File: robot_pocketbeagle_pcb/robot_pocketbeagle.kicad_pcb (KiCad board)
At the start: 2 copper layers, 75 x 100 mm, 104 parts, among them J1 QMC5883L, J10 driver_dvr8833, J12 IN_DVR8833, J13 9V_DC_DC, J14 servo_x_y, J15 shr05, J16 5V_DC_DC, J17 Conn_GND, J18 Conn_5V, J19 Conn_pwm_out_b, J2 USB_A, J20 Conn_pwm_out_a, J21 Conn_P2_3.3V, J29 Conn_AIN_4.096_3.3_1.8V, J3 UART0, J30 Conn_5V, J31 Conn_GPI028_34, J4 P1, J5 MPU6050, J6 ADS1115, J7 P2, J8 Conn_i2c2, J9 OUT_DVR8833, Q1 BC847, Q2 BC847, Q3 QM6015D, Q4 BC847, Q5 BC847, Q6 QM6015D, Q7 QM6015D, U1 PC817, U2 PC817, U3 74HC00, U4 LM358, U5 L7805_REZERV

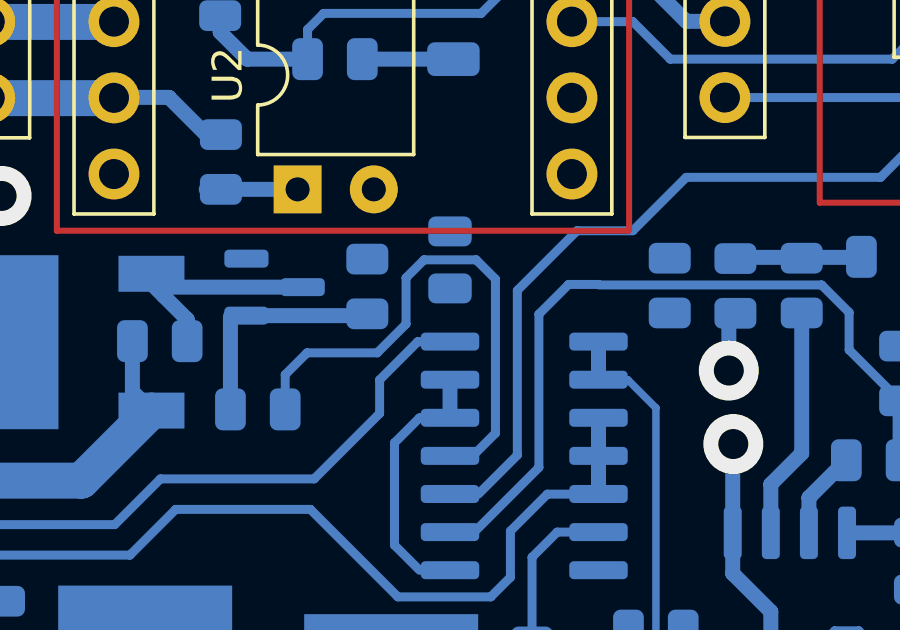
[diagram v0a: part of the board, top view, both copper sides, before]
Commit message: add doc and fix shem board
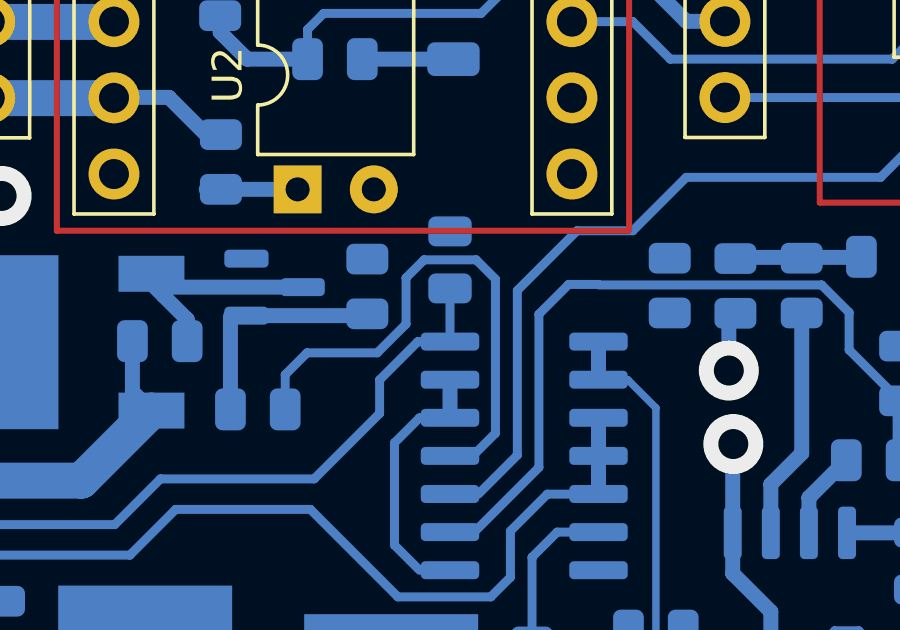
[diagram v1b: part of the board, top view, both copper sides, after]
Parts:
- C5: value 33n -> 330n
- C6: value 1n -> 100n
- R1, R2: value 1K -> 180
- R14: value 150K -> 1.5K
- R15: value 75K -> 750
- R16: value 430K -> 4.3K
- R17: value 100K -> 1K
- R18: value 110K -> 2k
- R21: value 100K -> 1.5k
- R30: value 110K -> 2K
- R31: value 100K -> 1.5K
- R41: value 2K -> 350
- R8: value 3K -> 3.3K
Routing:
- net AUX_5V_OUT: track 56.7 -> 58.4 mm
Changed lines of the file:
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@@
       (effects (font (size 1 1) (thickness 0.15)) (justify mirror))
     )
-    (fp_text value "430K" (at 0 -1.65 90) (layer "B.Fab")
+    (fp_text value "4.3K" (at 0 -1.65 90) (layer "B.Fab")
       (effects (font (size 1 1) (thickness 0.15)) (justify mirror))
     )
@@
       (effects (font (size 1 1) (thickness 0.15)) (justify mirror))
     )
-    (fp_text value "100K" (at 0 -1.65) (layer "B.Fab")
+    (fp_text value "1.5k" (at 0 -1.65) (layer "B.Fab")
       (effects (font (size 1 1) (thickness 0.15)) (justify mirror))
     )
@@
       (effects (font (size 1 1) (thickness 0.15)) (justify mirror))
     )
-    (fp_text value "33n" (at 0 -1.68 90) (layer "B.Fab")
+    (fp_text value "330n" (at 0 -1.68 90) (layer "B.Fab")
       (effects (font (size 1 1) (thickness 0.15)) (justify mirror))
     )
@@
       (effects (font (size 1 1) (thickness 0.15)) (justify mirror))
     )
-    (fp_text value "1n" (at 0 -1.68 90) (layer "B.Fab")
+    (fp_text value "100n" (at 0 -1.68 90) (layer "B.Fab")
       (effects (font (size 1 1) (thickness 0.15)) (justify mirror))
     )
@@
       (effects (font (size 1 1) (thickness 0.15)) (justify mirror))
     )
-    (fp_text value "3K" (at 0 -1.65 90) (layer "B.Fab")
+    (fp_text value "3.3K" (at 0 -1.65 90) (layer "B.Fab")
       (effects (font (size 1 1) (thickness 0.15)) (justify mirror))
     )
@@
       (effects (font (size 1 1) (thickness 0.15)) (justify mirror))
     )
-    (fp_text value "2K" (at 0 -1.65 90) (layer "B.Fab")
+    (fp_text value "350" (at 0 -1.65 90) (layer "B.Fab")
       (effects (font (size 1 1) (thickness 0.15)) (justify mirror))
     )
@@
       (effects (font (size 1 1) (thickness 0.15)) (justify mirror))
     )
-    (fp_text value "150K" (at 0 -1.65 90) (layer "B.Fab")
+    (fp_text value "1.5K" (at 0 -1.65 90) (layer "B.Fab")
       (effects (font (size 1 1) (thickness 0.15)) (justify mirror))
     )
@@
       (effects (font (size 1 1) (thickness 0.15)) (justify mirror))
     )
-    (fp_text value "75K" (at -4.1311 -5.0659) (layer "B.Fab")
+    (fp_text value "750" (at -4.1311 -5.0659) (layer "B.Fab")
       (effects (font (size 1 1) (thickness 0.15)) (justify mirror))
     )
@@
       (effects (font (size 1 1) (thickness 0.15)) (justify mirror))
     )
-    (fp_text value "100K" (at 0 -1.65 90) (layer "B.Fab")
+    (fp_text value "1.5K" (at 0 -1.65 90) (layer "B.Fab")
       (effects (font (size 1 1) (thickness 0.15)) (justify mirror))
     )
@@
       (effects (font (size 1 1) (thickness 0.15)) (justify mirror))
     )
-    (fp_text value "1K" (at 0 -1.65 90) (layer "B.Fab")
+    (fp_text value "180" (at 0 -1.65 90) (layer "B.Fab")
       (effects (font (size 1 1) (thickness 0.15)) (justify mirror))
     )
@@
       (effects (font (size 1 1) (thickness 0.15)) (justify mirror))
     )
-    (fp_text value "110K" (at 0 -1.65) (layer "B.Fab")
+    (fp_text value "2K" (at 0 -1.65) (layer "B.Fab")
       (effects (font (size 1 1) (thickness 0.15)) (justify mirror))
     )
@@
       (effects (font (size 1 1) (thickness 0.15)) (justify mirror))
     )
-    (fp_text value "1K" (at 0 -1.65 90) (layer "B.Fab")
+    (fp_text value "180" (at 0 -1.65 90) (layer "B.Fab")
       (effects (font (size 1 1) (thickness 0.15)) (justify mirror))
     )
@@
       (effects (font (size 1 1) (thickness 0.15)) (justify mirror))
     )
-    (fp_text value "100K" (at 0 -1.65) (layer "B.Fab")
+    (fp_text value "1K" (at 0 -1.65) (layer "B.Fab")
       (effects (font (size 1 1) (thickness 0.15)) (justify mirror))
     )
@@
       (effects (font (size 1 1) (thickness 0.15)) (justify mirror))
     )
-    (fp_text value "110K" (at 0 -1.65) (layer "B.Fab")
+    (fp_text value "2k" (at 0 -1.65) (layer "B.Fab")
       (effects (font (size 1 1) (thickness 0.15)) (justify mirror))
     )
@@
   (segment (start 105.664 102.616) (end 104.648 103.632) (width 0.3) (layer "B.Cu") (net 54))
   (segment (start 111.1 116.18) (end 112.66 116.18) (width 0.5) (layer "B.Cu") (net 54))
+  (segment (start 122.936 94.742) (end 122.936 96.515) (width 0.3) (layer "B.Cu") (net 54))
   (segment (start 112.73 114.91) (end 112.73 116.11) (width 0.6) (layer "B.Cu") (net 54))
   (segment (start 110.495 114.147) (end 109.927 114.715) (width 0.3) (layer "B.Cu") (net 54))

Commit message: fix board
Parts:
- R1, R2: value 180 -> 300
- R22, R23: value 2K -> 1K
- R4, R5: value 47k -> 1k
- R41: value 350 -> 680
- R48, R52: value 90k -> 1.5k
- R8: value 3.3K -> 2.4K
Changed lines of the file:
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@@
       (effects (font (size 1 1) (thickness 0.15)) (justify mirror))
     )
-    (fp_text value "3.3K" (at 0 -1.65 90) (layer "B.Fab")
+    (fp_text value "2.4K" (at 0 -1.65 90) (layer "B.Fab")
       (effects (font (size 1 1) (thickness 0.15)) (justify mirror))
     )
@@
       (effects (font (size 1 1) (thickness 0.15)) (justify mirror))
     )
-    (fp_text value "2K" (at 0 -1.65 90) (layer "B.Fab")
+    (fp_text value "1K" (at 0 -1.65 90) (layer "B.Fab")
       (effects (font (size 1 1) (thickness 0.15)) (justify mirror))
     )
@@
       (effects (font (size 1 1) (thickness 0.15)) (justify mirror))
     )
-    (fp_text value "350" (at 0 -1.65 90) (layer "B.Fab")
+    (fp_text value "680" (at 0 -1.65 90) (layer "B.Fab")
       (effects (font (size 1 1) (thickness 0.15)) (justify mirror))
     )
@@
       (effects (font (size 1 1) (thickness 0.15)) (justify mirror))
     )
-    (fp_text value "180" (at 0 -1.65 90) (layer "B.Fab")
+    (fp_text value "300" (at 0 -1.65 90) (layer "B.Fab")
       (effects (font (size 1 1) (thickness 0.15)) (justify mirror))
     )
@@
       (effects (font (size 1 1) (thickness 0.15)) (justify mirror))
     )
-    (fp_text value "90k" (at 0 -1.65 90) (layer "B.Fab")
+    (fp_text value "1.5k" (at 0 -1.65 90) (layer "B.Fab")
       (effects (font (size 1 1) (thickness 0.15)) (justify mirror))
     )
@@
       (effects (font (size 1 1) (thickness 0.15)) (justify mirror))
     )
-    (fp_text value "90k" (at 0 -1.65) (layer "B.Fab")
+    (fp_text value "1.5k" (at 0 -1.65) (layer "B.Fab")
       (effects (font (size 1 1) (thickness 0.15)) (justify mirror))
     )
@@
       (effects (font (size 1 1) (thickness 0.15)) (justify mirror))
     )
-    (fp_text value "180" (at 0 -1.65 90) (layer "B.Fab")
+    (fp_text value "300" (at 0 -1.65 90) (layer "B.Fab")
       (effects (font (size 1 1) (thickness 0.15)) (justify mirror))
     )
@@
       (effects (font (size 1 1) (thickness 0.15)) (justify mirror))
     )
-    (fp_text value "47k" (at 0 -1.65 90) (layer "B.Fab")
+    (fp_text value "1k" (at 0 -1.65 90) (layer "B.Fab")
       (effects (font (size 1 1) (thickness 0.15)) (justify mirror))
     )
@@
       (effects (font (size 1 1) (thickness 0.15)) (justify mirror))
     )
-    (fp_text value "2K" (at 0 -1.65) (layer "B.Fab")
+    (fp_text value "1K" (at 0 -1.65) (layer "B.Fab")
       (effects (font (size 1 1) (thickness 0.15)) (justify mirror))
     )
@@
       (effects (font (size 1 1) (thickness 0.15)) (justify mirror))
     )
-    (fp_text value "47k" (at 0 -1.65) (layer "B.Fab")
-      (effects (font (size 1 1) (thickness 0.15)) (justify mirror))
-    )
+    (fp_text value "1k" (at 0 -1.65) (layer "B.Fab")
+      (effects (font (size 1 1) (thickness 0.15)) (justify mirror))
+    )
